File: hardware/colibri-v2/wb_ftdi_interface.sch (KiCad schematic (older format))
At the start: 12 parts

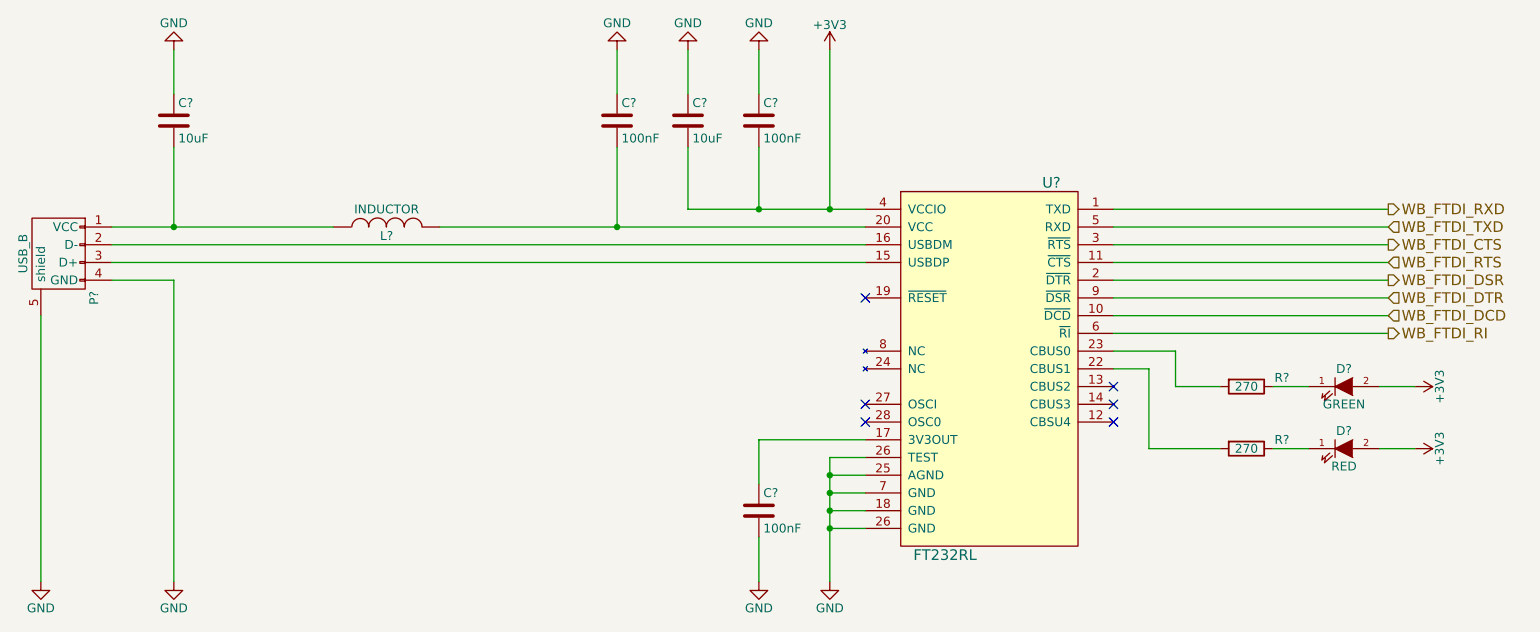
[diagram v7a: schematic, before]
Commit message: Work on wandboard lcd and usb
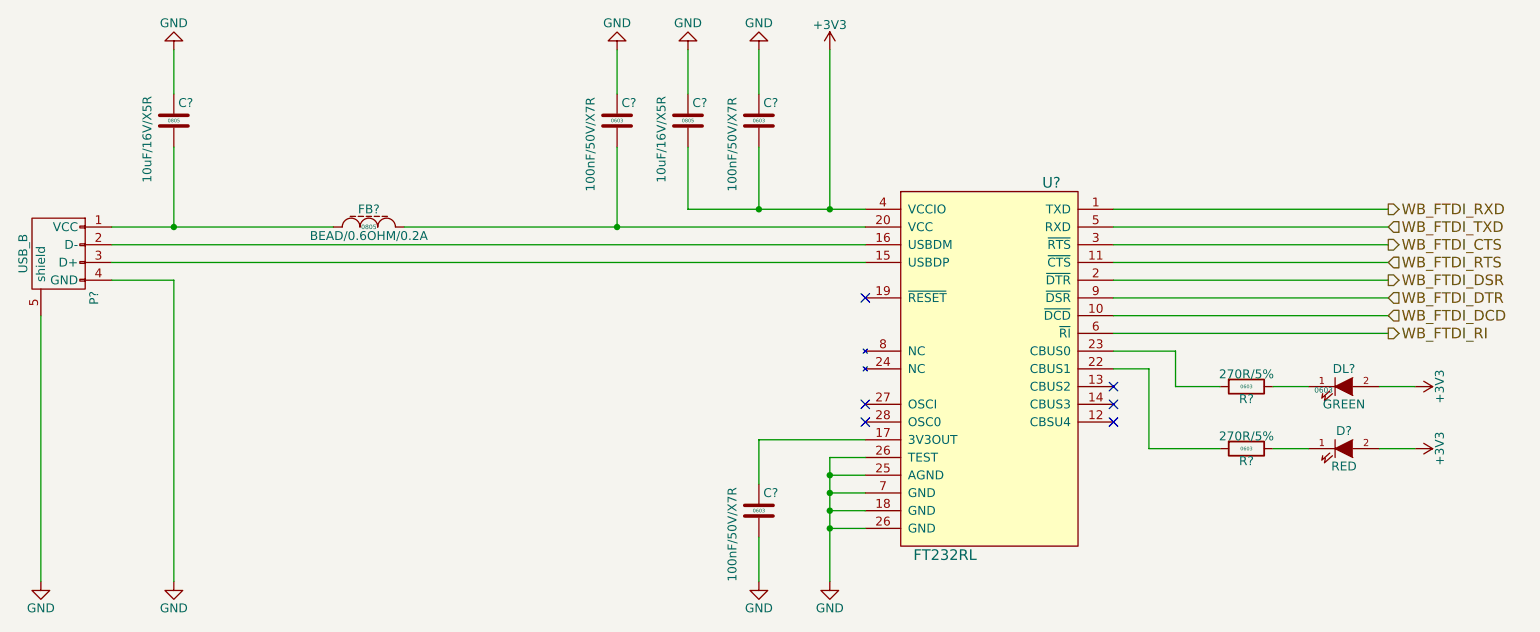
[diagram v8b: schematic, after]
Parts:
- removed C? (x3): 100nF, Capacitors_SMD:C_0805, symbol C
- removed C? (x2): 10uF, Capacitors_SMD:C_0805, symbol C
- removed D?: GREEN, symbol LED
- removed D?: RED, symbol LED
- removed L?: INDUCTOR, symbol INDUCTOR
- removed R? (x2): 270, Resistors_SMD:R_0603, symbol R
- added C? (x3): 100nF/50V/X7R, Capacitors_SMD:C_0603, symbol C_SMT
- added C? (x2): 10uF/16V/X5R, Capacitors_SMD:C_0603, symbol C_SMT
- added D?: RED, symbol LED
- added DL?: GREEN, LEDs:LED-0603, symbol LED_SMT
- added FB?: BEAD/0.6OHM/0.2A, Resistors_SMD:R_0805, symbol FB_SMT
- added R? (x2): 270R/5%, Resistors_SMD:R_0603, symbol R_SMT
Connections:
- net +3V3: now also C?.2, C?.2, D?.2 (A), DL?.2 (A)
- net GND: now also C?.1, C?.1, C?.1, C?.1, C?.2
- net at U?.17 (3V3OUT): now also C?.1
- net at U?.20 (VCC): now also C?.2, FB?.2
- net at U?.22 (CBUS1): now also R?.2
- net at U?.23 (CBUS0): now also R?.2
- net at P?.1 (VCC): now also C?.2, FB?.1
- new net: DL?.1 (K), R?.1
- new net: D?.1 (K), R?.1
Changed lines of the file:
@@
 	0    -1   1    0
 $EndComp
-$Comp
-L INDUCTOR L?
-U 1 1 560A13B6
-P 3600 3350
-F 0 "L?" V 3550 3350 50  0000 C CNN
-F 1 "INDUCTOR" V 3700 3350 50  0000 C CNN
-F 2 "" H 3600 3350 60  0001 C CNN
-F 3 "" H 3600 3350 60  0000 C CNN
-	1    3600 3350
-	0    -1   -1   0
-$EndComp
-Wire Wire Line
-	2050 3350 3300 3350
-Wire Wire Line
-	3900 3350 6300 3350
+Wire Wire Line
+	2050 3350 2400 3350
+Wire Wire Line
+	2400 3350 3300 3350
+Wire Wire Line
+	3700 3350 4900 3350
+Wire Wire Line
+	4900 3350 6300 3350
 Wire Wire Line
 	2050 3450 6300 3450
@@
 	6300 4650 6100 4650
 Wire Wire Line
-	6100 4650 6100 5350
+	6100 4650 6100 4750
+Wire Wire Line
+	6100 4750 6100 4850
+Wire Wire Line
+	6100 4850 6100 4950
+Wire Wire Line
+	6100 4950 6100 5050
+Wire Wire Line
+	6100 5050 6100 5350
 Wire Wire Line
 	6300 4750 6100 4750
@@
 	6100 5050 6300 5050
 Connection ~ 6100 5050
-$Comp
-L C C?
-U 1 1 560A13D1
-P 5700 4950
-F 0 "C?" H 5725 5050 50  0000 L CNN
-F 1 "100nF" H 5725 4850 50  0000 L CNN
-F 2 "Capacitors_SMD:C_0805" H 5738 4800 30  0001 C CNN
-F 3 "" H 5700 4950 60  0000 C CNN
-	1    5700 4950
-	1    0    0    -1
-$EndComp
 Wire Wire Line
 	6300 4550 5700 4550
@@
 $EndComp
 $Comp
-L C C?
-U 1 1 560A13E7
-P 5700 2750
-F 0 "C?" H 5725 2850 50  0000 L CNN
-F 1 "100nF" H 5725 2650 50  0000 L CNN
-F 2 "Capacitors_SMD:C_0805" H 5738 2600 30  0001 C CNN
-F 3 "" H 5700 2750 60  0000 C CNN
-	1    5700 2750
-	1    0    0    -1
-$EndComp
-$Comp
 L GND #PWR?
 U 1 1 560A13EE
@@
 	5700 2900 5700 3250
 $Comp
-L C C?
-U 1 1 560A13F6
-P 5300 2750
-F 0 "C?" H 5325 2850 50  0000 L CNN
-F 1 "10uF" H 5325 2650 50  0000 L CNN
-F 2 "Capacitors_SMD:C_0805" H 5338 2600 30  0001 C CNN
-F 3 "" H 5300 2750 60  0000 C CNN
-	1    5300 2750
-	1    0    0    -1
-$EndComp
-$Comp
 L GND #PWR?
 U 1 1 560A13FD
@@
 Connection ~ 5700 3250
 $Comp
-L C C?
-U 1 1 560A1406
-P 2400 2750
-F 0 "C?" H 2425 2850 50  0000 L CNN
-F 1 "10uF" H 2425 2650 50  0000 L CNN
-F 2 "Capacitors_SMD:C_0805" H 2438 2600 30  0001 C CNN
-F 3 "" H 2400 2750 60  0000 C CNN
-	1    2400 2750
-	1    0    0    -1
-$EndComp
-$Comp
-L C C?
-U 1 1 560A140D
-P 4900 2750
-F 0 "C?" H 4925 2850 50  0000 L CNN
-F 1 "100nF" H 4925 2650 50  0000 L CNN
-F 2 "Capacitors_SMD:C_0805" H 4938 2600 30  0001 C CNN
-F 3 "" H 4900 2750 60  0000 C CNN
-	1    4900 2750
-	1    0    0    -1
-$EndComp
-$Comp
 L GND #PWR?
 U 1 1 560A1414
@@
 	6100 3250 6100 2350
 Wire Wire Line
-	5300 3250 6300 3250
+	5300 3250 5700 3250
+Wire Wire Line
+	5700 3250 6100 3250
+Wire Wire Line
+	6100 3250 6300 3250
 Connection ~ 6100 3250
 Text HLabel 9250 3250 2    60   Output ~ 0
@@
 	7700 3950 9250 3950
 $Comp
-L LED D?
-U 1 1 560A1448
-P 9000 4250
-F 0 "D?" H 9000 4350 50  0000 C CNN
-F 1 "GREEN" H 9000 4150 50  0000 C CNN
-F 2 "" H 9000 4250 60  0001 C CNN
-F 3 "" H 9000 4250 60  0000 C CNN
-	1    9000 4250
-	1    0    0    -1
-$EndComp
-$Comp
-L R R?
-U 1 1 560A144F
-P 8450 4250
-F 0 "R?" V 8400 4450 50  0000 C CNN
-F 1 "270" V 8450 4250 50  0000 C CNN
-F 2 "Resistors_SMD:R_0603" V 8380 4250 30  0001 C CNN
-F 3 "" H 8450 4250 30  0000 C CNN
-	1    8450 4250
-	0    1    1    0
-$EndComp
-$Comp
 L +3V3 #PWR?
 U 1 1 560A1456
@@
 	9200 4250 9400 4250
 $Comp
-L LED D?
-U 1 1 560A145E
-P 9000 4600
-F 0 "D?" H 9000 4700 50  0000 C CNN
-F 1 "RED" H 9000 4500 50  0000 C CNN
-F 2 "" H 9000 4600 60  0001 C CNN
-F 3 "" H 9000 4600 60  0000 C CNN
-	1    9000 4600
-	1    0    0    -1
-$EndComp
-$Comp
-L R R?
-U 1 1 560A1465
-P 8450 4600
-F 0 "R?" V 8400 4800 50  0000 C CNN
-F 1 "270" V 8450 4600 50  0000 C CNN
-F 2 "Resistors_SMD:R_0603" V 8380 4600 30  0001 C CNN
-F 3 "" H 8450 4600 30  0000 C CNN
-	1    8450 4600
-	0    1    1    0
-$EndComp
-$Comp
 L +3V3 #PWR?
 U 1 1 560A146C
@@
 Wire Wire Line
 	7700 3850 9250 3850
+$Comp
+L R_SMT R?
+U 1 1 56335349
+P 8450 4250
+F 0 "R?" V 8520 4250 50  0000 C CNN
+F 1 "270R/5%" V 8380 4250 50  0000 C CNN
+F 2 "Resistors_SMD:R_0603" V 8600 4250 30  0001 C CNN
+F 3 "" V 8530 4250 30  0000 C CNN
+F 4 "0603" V 8450 4250 20  0000 C CNN "SMT"
+F 5 "9330917" V 8650 4250 30  0001 C CNN "Part"
+F 6 "Farnell" V 8700 4250 30  0001 C CNN "Provider"
+	1    8450 4250
+	0    1    1    0
+$EndComp
+$Comp
+L R_SMT R?
+U 1 1 5633542F
+P 8450 4600
+F 0 "R?" V 8520 4600 50  0000 C CNN
+F 1 "270R/5%" V 8380 4600 50  0000 C CNN
+F 2 "Resistors_SMD:R_0603" V 8600 4600 30  0001 C CNN
+F 3 "" V 8530 4600 30  0000 C CNN
+F 4 "0603" V 8450 4600 20  0000 C CNN "SMT"
+F 5 "9330917" V 8650 4600 30  0001 C CNN "Part"
+F 6 "Farnell" V 8700 4600 30  0001 C CNN "Provider"
+	1    8450 4600
+	0    1    1    0
+$EndComp
+$Comp
+L LED_SMT DL?
+U 1 1 5633554F
+P 9000 4250
+F 0 "DL?" H 9000 4350 50  0000 C CNN
+F 1 "GREEN" H 9000 4150 50  0000 C CNN
+F 2 "LEDs:LED-0603" H 9000 4100 30  0001 C CNN
+F 3 "" H 9000 4250 60  0000 C CNN
+F 4 "0603" H 8885 4230 30  0000 C CNN "SMT"
+F 5 "2322070" H 9000 4050 30  0001 C CNN "Part"
+F 6 "Farnell" H 9000 4000 30  0001 C CNN "Provider"
+	1    9000 4250
+	1    0    0    -1
+$EndComp
+$Comp
+L LED D?
+U 1 1 56335832
+P 9000 4600
+F 0 "D?" H 9000 4700 50  0000 C CNN
+F 1 "RED" H 9000 4500 50  0000 C CNN
+F 2 "" H 9000 4600 60  0001 C CNN
+F 3 "" H 9000 4600 60  0000 C CNN
+	1    9000 4600
+	1    0    0    -1
+$EndComp
+$Comp
+L C_SMT C?
+U 1 1 56335D21
+P 5700 4950
+F 0 "C?" H 5725 5050 50  0000 L CNN
+F 1 "100nF/50V/X7R" V 5550 4550 50  0000 L CNN
+F 2 "Capacitors_SMD:C_0603" H 5730 4800 30  0001 L CNN
+F 3 "" H 5725 5050 60  0000 L CNN
+F 4 "0603" H 5700 4950 20  0000 C CNN "SMT"
+F 5 "1414028" H 5730 4760 30  0001 L CNN "Part"
+F 6 "Farnell" H 5730 4720 30  0001 L CNN "Provider"
+	1    5700 4950
+	1    0    0    -1
+$EndComp
+$Comp
+L FB_SMT FB?
+U 1 1 56336479
+P 3500 3350
+F 0 "FB?" H 3500 3450 50  0000 C CNN
+F 1 "BEAD/0.6OHM/0.2A" H 3500 3300 50  0000 C CNN
+F 2 "Resistors_SMD:R_0805" H 3500 3250 30  0001 C CNN
+F 3 "" H 3550 3350 60  0000 C CNN
+F 4 "0805" H 3500 3350 25  0000 C CNN "SMT"
+F 5 "1515714" H 3500 3200 30  0001 C CNN "Part"
+F 6 "Farnell" H 3500 3150 30  0001 C CNN "Provider"
+	1    3500 3350
+	1    0    0    -1
+$EndComp
+$Comp
+L C_SMT C?
+U 1 1 5633664F
+P 2400 2750
+F 0 "C?" H 2425 2850 50  0000 L CNN
+F 1 "10uF/16V/X5R" V 2250 2400 50  0000 L CNN
+F 2 "Capacitors_SMD:C_0603" H 2430 2600 30  0001 L CNN
+F 3 "" H 2425 2850 60  0000 L CNN
+F 4 "0805" H 2400 2750 20  0000 C CNN "SMT"
+F 5 "1762635" H 2430 2560 30  0001 L CNN "Part"
+F 6 "Farnell" H 2430 2520 30  0001 L CNN "Provider"
+	1    2400 2750
+	1    0    0    -1
+$EndComp
+$Comp
+L C_SMT C?
+U 1 1 5633687F
+P 5300 2750
+F 0 "C?" H 5325 2850 50  0000 L CNN
+F 1 "10uF/16V/X5R" V 5150 2400 50  0000 L CNN
+F 2 "Capacitors_SMD:C_0603" H 5330 2600 30  0001 L CNN
+F 3 "" H 5325 2850 60  0000 L CNN
+F 4 "0805" H 5300 2750 20  0000 C CNN "SMT"
+F 5 "1762635" H 5330 2560 30  0001 L CNN "Part"
+F 6 "Farnell" H 5330 2520 30  0001 L CNN "Provider"
+	1    5300 2750
+	1    0    0    -1
+$EndComp
+$Comp
+L C_SMT C?
+U 1 1 563369C6
+P 5700 2750
+F 0 "C?" H 5725 2850 50  0000 L CNN
+F 1 "100nF/50V/X7R" V 5550 2350 50  0000 L CNN
+F 2 "Capacitors_SMD:C_0603" H 5730 2600 30  0001 L CNN
+F 3 "" H 5725 2850 60  0000 L CNN
+F 4 "0603" H 5700 2750 20  0000 C CNN "SMT"
+F 5 "1414028" H 5730 2560 30  0001 L CNN "Part"
+F 6 "Farnell" H 5730 2520 30  0001 L CNN "Provider"
+	1    5700 2750
+	1    0    0    -1
+$EndComp
+$Comp
+L C_SMT C?
+U 1 1 56336BEE
+P 4900 2750
+F 0 "C?" H 4925 2850 50  0000 L CNN
+F 1 "100nF/50V/X7R" V 4750 2350 50  0000 L CNN
+F 2 "Capacitors_SMD:C_0603" H 4930 2600 30  0001 L CNN
+F 3 "" H 4925 2850 60  0000 L CNN
+F 4 "0603" H 4900 2750 20  0000 C CNN "SMT"
+F 5 "1414028" H 4930 2560 30  0001 L CNN "Part"
+F 6 "Farnell" H 4930 2520 30  0001 L CNN "Provider"
+	1    4900 2750
+	1    0    0    -1
+$EndComp
 $EndSCHEMATC
